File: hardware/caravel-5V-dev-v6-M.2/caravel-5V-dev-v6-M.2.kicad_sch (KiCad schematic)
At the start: 75 parts, among them J1 USB_B_Micro - 10118193-0001LF, J10 Conn_01x02_Male, J11 Conn_01x20_Female, J12 Conn_01x27_Female, J13 Conn_01x02_Male, J2 Conn_01x02_Female, J3 Conn_01x02_Male, J4 Conn_01x03_Female, J5 Conn_01x02_Male, J6 Conn_01x02_Male, J7 Conn_01x06_Female, J8 Conn_01x02_Male, J9 Conn_01x02_Male, SW1 SW_Push - SKQGADE010, T1 Logo, T2 Logo, U1 FT232H, U10 TXB0104PWR, U2 SN74LVC1G125DCKR, U3 SN74LVC1G125DCKR, U4 MCP1319MT-29LE-OT, U5 TAR5SxxU_SOT353F, U6 TXB0104PWR, U7 W25Q32FVSS, U8 caravel-M.2-card, U9 TXB0104PWR, X1 SG7050CCN_10MHZ, Y1 CSTNE12M0GH5L000R0

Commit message: update 5V development board (REV 6B) schematic: ~ fix the reversed connections on the U10 level shifter + add 1 and 0.01 uF bypass caps to the Flash memory supply + add 10 uF bulk decoupling cap to the FTDI supply + add 100K pull-up resistor on the ~{MR} ~ update pull-up resistors of the Flash and ~{UART_EN} to 100K ~ update LEDs resistors to 10K
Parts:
- removed R17, R18: 10k - RC0805FR-0710KL, Resistor_SMD:R_0805_2012Metric, symbol Device:R
- added C23, C25: 0.1uf - CC0805KRX7R9BB104, Capacitor_SMD:C_0805_2012Metric, symbol Device:C
- added C26: 0.01uf - CC0805KRX7R9BB103, Capacitor_SMD:C_0805_2012Metric, symbol Device:C
- added C27: 1uf - CC0805KKX5R8BB105, Capacitor_SMD:C_0805_2012Metric, symbol Device:C
- added U11: MCP1319MT-29LE-OT, Caravel_Board:PoR_5_SOT23, symbol Caravel_board:MCP1319MT-29LE-OT
- C16: value 0.1uf - CC0805KRX7R9BB104 -> 10uf - CC0805KKX5R8BB106
- J10, J13, J3, J5, J6, J8, J9: value Conn_01x02_Male -> Conn_01x02_Pin; symbol Connector:Conn_01x02_Male -> Connector:Conn_01x02_Pin
- J11, J12: symbol Connector:Conn_01x28_Female -> Connector:Conn_01x28_Socket
- J2: symbol Connector:Conn_01x02_Female -> Connector:Conn_01x02_Socket
- J7: symbol Connector:Conn_01x06_Female -> Connector:Conn_01x06_Socket
- R10, R11, R16, R5, R6, R7, R8: value 10k - RC0805FR-0710KL -> 100K - RC0805FR-07100KL
- R13, R14: value 1K - RC0805FR-071KL -> 10k - RC0805FR-0710KL
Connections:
- net +5V: now also R16.1
- net GND: now also C16.1, C23.1, C25.2, C26.1, C27.2, U11.2 (VSS); no longer C16.2
- net USB_SCK_TXD_H: now also U10.10 (B4); no longer U10.11 (B3)
- net USB_SO_RXD_H: now also U10.11 (B3); no longer U10.10 (B4)
- net ~{MR}: now also R16.2
- net at C1.2, U1.34 (~{RESET}): now also R1.2; no longer R1.1
- net OE: now reaches U10.8 (OE)
- net OE: now also U6.8 (OE), U9.8 (OE), U11.1 (~{RST})
- net +3.3V renamed +3V3
- net +3V3: now also C16.2, R1.1, C23.2, C25.1, C26.2, C27.1, U11.5 (VDD); no longer C16.1, R1.2, R16.1
- net UART_EN renamed ~{UART_EN}
- net UART_EN_L renamed ~{UART_EN}_L
- no-connect marks 26 -> 28
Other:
- note added: "Caravel M.2 Card"
- note added: "FTDI SPI interface with HKSPI"
- note added: "FTDI UART interface with Caravel"
- note added: "Flash memory interface with Caravel Flash SPI"
- note added: "GPIO Connectors"
- note added: "Interfaces"
- note added: "Pin Headers"
- note added: "Power Supplies"
- note added: "Reset Switch"
- note removed: "FTDI interface with HKSPI"
- note removed: "Flash memory interface with Caravel"
- note removed: "IO Connectors"
- note removed: "Power Pin Headers"
- moved on the sheet: C1, C10, C11, C12, C13, C14, C15, C17, C18, C19, C2, C20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

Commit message: update `caravel-5V-dev-v6-M.2` to REV6B that fixes identified issues during bringup
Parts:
- removed C17, C18, C19, C20, C23: 0.1uf - CC0805KRX7R9BB104, Capacitor_SMD:C_0805_2012Metric, symbol Device:C
- removed U10, U6, U9: TXB0104PWR, Package_SO:TSSOP-14_4.4x5mm_P0.65mm, symbol Logic_LevelTranslator:TXB0104PW
- removed U11: MCP1319MT-29LE-OT, Caravel_Board:PoR_5_SOT23, symbol Caravel_board:MCP1319MT-29LE-OT
- added C13: 0.01uF, Capacitor_SMD:C_0805_2012Metric, symbol Device:C
- added FB1: 600R/0.5A, Inductor_SMD:L_0805_2012Metric, symbol Device:FerriteBead
- added J14, J15, J16: Conn_01x02_Pin, Connector_PinHeader_2.54mm:PinHeader_1x02_P2.54mm_Vertical, symbol Connector:Conn_01x02_Pin
- added Q1: IRLML6402, Package_TO_SOT_SMD:SOT-23, symbol Transistor_FET:IRLML6402
- added R17, R19: 10K, Resistor_SMD:R_0805_2012Metric, symbol Device:R
- added R18: 2K, Resistor_SMD:R_0805_2012Metric, symbol Device:R
- added R20: 100K, Resistor_SMD:R_0805_2012Metric, symbol Device:R
- added U10, U11, U12, U6, U9: SN74LV1T34DCK, Package_TO_SOT_SMD:SOT-353_SC-70-5, symbol Logic_LevelTranslator:SN74LV1T34DCK
- C1: value 0.01uf - CC0805JRX7R9BB103 -> 0.01uF; Part # (none) -> C0805C103K5RAC7411
- C10: value 1uf - CC0805KKX5R8BB105 -> 1uf; Part # (none) -> 885012207103
- C11: value 0.01uf - CC0805KRX7R9BB103 -> 0.01uF; Part # (none) -> C0805C103K5RAC7411
- C12: value 10uf - CC0805KKX5R8BB106 -> 10uf; Part # (none) -> CL21B106KAYQNNE
- C14: renamed from C13; value 0.1uf - CC0805KRX7R9BB104 -> 0.1uF; Part # (none) -> C0805C104K5RAC7411
- C15, C2, C21, C22, C3, C4, C5, C6, C7, C8, C9: value 0.1uf - CC0805KRX7R9BB104 -> 0.1uF; Part # (none) -> C0805C104K5RAC7411
- C16: renamed from C25; value 0.1uf - CC0805KRX7R9BB104 -> 0.1uF; Part # (none) -> C0805C104K5RAC7411
- C17: renamed from C26; value 0.01uf - CC0805KRX7R9BB103 -> 0.01uF; Part # (none) -> C0805C103K5RAC7411
- C18: renamed from C27; value 1uf - CC0805KKX5R8BB105 -> 1uf; Part # (none) -> 885012207103
- C19: renamed from C16; value 10uf - CC0805KKX5R8BB106 -> 10uf; Part # (none) -> CL21B106KAYQNNE
- C20: renamed from C14; value 10uf - CC0805KKX5R8BB106 -> 10uf; Part # (none) -> CL21B106KAYQNNE
- D1, D2, D3, D4: value LED - 17-215SURC/S530-A2/TR8 -> RED; Part # (none) -> LTST-C230KRKT
- J1: value USB_B_Micro - 10118193-0001LF -> USB_B_Micro; Part # (none) -> 10118193-0001LF
- J11: value Conn_01x20_Female -> Conn_01x28_Pin; footprint Connector_PinHeader_2.54mm:PinHeader_1x20_P2.54mm_Vertical -> Connector_PinHeader_2.54mm:PinHeader_1x28_P2.54mm_Vertical
- J12: value Conn_01x27_Female -> Conn_01x28_Pin; footprint Connector_PinHeader_2.54mm:PinHeader_1x27_P2.54mm_Vertical -> Connector_PinHeader_2.54mm:PinHeader_1x28_P2.54mm_Vertical
- J2: value Conn_01x02_Female -> Conn_01x02_Pin; symbol Connector:Conn_01x02_Socket -> Connector:Conn_01x02_Pin
- J4: value Conn_01x03_Female -> Conn_01x03_Pin
- J7: value Conn_01x06_Female -> Conn_01x06_Pin; symbol Connector:Conn_01x06_Socket -> Connector:Conn_01x06_Pin
- R1, R12, R13, R14, R15, R9: value 10k - RC0805FR-0710KL -> 10K; Part # (none) -> RC0805FR-0710KL
- R10, R11, R7, R8: value 100K - RC0805FR-07100KL -> 100K; Part # (none) -> RC0805FR-07100KL
- R16, R5, R6: value 100K - RC0805FR-07100KL -> 10K; Part # (none) -> RC0805FR-0710KL
- R2: value 12K 1% - 0805W8F1202T5E -> 12K 1%; Part # (none) -> RMCF0805FT12K0
- R3, R4: value 150 - 0805W8J0151T5E -> 150; Part # (none) -> RNCP0805FTD150R
- U1: Part # (none) -> FT232H
- U2, U3: Field4 76C4082 -> (none); Field5 Texas Instruments -> (none); Field6 SN74LVC1G125DCKR -> (none); Field7 1470771 -> (none); Part # (none) -> SN74LVC1G125DCKR
- U4: Part # (none) -> MCP1319MT-29LE-OT
- U5: value TAR5SxxU_SOT353F -> TAR5SxxU; Part # (none) -> TAR5S33UTE85LF
- U7: Part # (none) -> W25Q32JVSSIQ
- U8: value caravel-M.2-card -> M.2-CONNECTOR-E; symbol Caravel_board:caravel-M.2-card -> MicroMod-Sparkfun:M.2-CONNECTOR-E
- X1: Part # (none) -> SG7050CCN-10-000000M-HJGA3
- Y1: value CSTNE12M0GH5L000R0 -> 12MHz; Part # (none) -> CSTNE12M0GH5L000R0
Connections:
- net USB_SCK_TXD_H is gone; now on net USB_SCK_TXD: U3.2 (A)
- net USB_SO_RXD_H is gone; now on net USB_SO_RXD: U2.4 (Y)
- net mprj_io[1]_SDO is gone; now on net USB_SI: J11.14 (Pin_14), U8.51 (P43)
- net mprj_io[2]_SDI is gone; now on net USB_SO_RXD: J11.13 (Pin_13), U8.53 (P45)
- net mprj_io[3]_CSB is gone; now on net USB_CS1: J11.12 (Pin_12), U8.55 (P47)
- net mprj_io[4]_SCK is gone; now on net USB_SCK_TXD: J11.11 (Pin_11), U8.57 (P49)
- net ~{MR}_L is gone; now on net ~{MR}: U1.25 (ACBUS1)
- net ~{UART_EN}_L is gone; now on net ~{UART_EN}: U1.21 (ACBUS0)
- net +3V3: now also C19.1, C4.1, C5.1, C6.1, C7.1, C8.1, R5.1, R6.1, U2.5 (VCC), U3.5 (VCC), R20.1, U10.5 (VCC), U6.5 (VCC), U9.5 (VCC); no longer C19.2, C21.2, C4.2, C5.2, C6.2, C7.2, C8.2
- net +5V: now also C14.2, C15.1, FB1.2, Q1.2 (S), R17.2, U11.5 (VCC), U12.5 (VCC); no longer C14.1, C15.2, C22.2, J1.1 (VBUS), J10.1 (Pin_1), J10.2 (Pin_2), J11.22 (Pin_22), J11.23 (Pin_23), J11.24 (Pin_24), J12.7 (Pin_7), J13.1 (Pin_1), J13.2 (Pin_2), J3.1 (Pin_1), J3.2 (Pin_2), J5.1 (Pin_1), J5.2 (Pin_2), J9.1 (Pin_1), J9.2 (Pin_2), R5.1, R6.1, U2.5 (VCC), U3.5 (VCC), U8.14 (vccd), U8.15 (vcdd), U8.16 (vddio), U8.3 (vddio), U8.35 (vccd1), U8.5 (vdda)
- net Caravel_CSB: now also U6.2 (A)
- net Caravel_D0: now also U10.2 (A)
- net Caravel_D1: now also U11.4 (Y)
- net Caravel_SCK: now also U9.2 (A)
- net GND: now also C14.1, C15.2, C19.2, C4.2, C5.2, C6.2, C7.2, C8.2, C13.2, R19.1, U10.3 (GND), U11.3 (GND), U12.3 (GND), U6.3 (GND), U9.3 (GND); no longer C14.2, C15.1, C19.1, C21.1, C4.1, C5.1, C6.1, C7.1, C8.1
- net MEM_SCK: now also U9.4 (Y)
- net MEM_SI: now also U10.4 (Y)
- net MEM_SO: now also U11.2 (A)
- net USB_SI: now also J16.1 (Pin_1), J16.2 (Pin_2), R20.2
- net ~{MR}: now also J14.2 (Pin_2)
- net ~{RST}: now also J14.1 (Pin_1)
- net VCCA: now reaches C3.2, U1.37 (VCCA)
- net Noise: now reaches C11.1, U5.3 (Noise)
- net ~{FTDI_RST}: now reaches C1.2, R1.2, U1.34 (~{RESET})
- net VCCCORE: now reaches C2.2, U1.38 (VCCCORE)
- net ~{PWR_EN}: now reaches U1.33 (ACBUS9)
- net ~{PWR_EN}: now also J15.1 (Pin_1), J15.2 (Pin_2), R19.2, U12.2 (A)
- net MEM_CS renamed ~{MEM_CS}
- net ~{MEM_CS}: now also U6.4 (Y)
- new net: C21.1, Q1.1 (G), R17.1, R18.2
- new net VBUS: C13.1, FB1.1, J1.1 (VBUS), J13.1 (Pin_1), J13.2 (Pin_2)
- new net VCC: C21.2, C22.2, J10.1 (Pin_1), J10.2 (Pin_2), J11.22 (Pin_22), J11.23 (Pin_23), J11.24 (Pin_24), J12.7 (Pin_7), J3.1 (Pin_1), J3.2 (Pin_2), J5.1 (Pin_1), J5.2 (Pin_2), J9.1 (Pin_1), J9.2 (Pin_2), Q1.3 (D), U8.14 (P14), U8.15 (P15), U8.16 (P16), U8.3 (P3), U8.35 (P27), U8.5 (P5)
- new net ~{PWR_EN}_H: R18.1, U12.4 (Y)
- no-connect marks 28 -> 25
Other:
- note added: "*Caravel power is turned on by default and the FTDI controls ~{PWR_EN}"
- note added: "*J16 ensures HKSPI SDO state when it's left high-impedance"
- note added: "*Place close to the USB connector"
- note added: "*required since the FTDI UART ports are shared with the SPI"
- note added: "*skips installing the PoR"
- note added: "Buffers to enable FTDI UART interface with Caravel"
- note added: "M.2 Connector + Peripherals"
- note added: "Power"
- note added: "Power Cycle Control"
- note added: "Reset"
- note added: "Reset Pin Header"
- note added: "USB to Serial"
- note added: "Use J15 to control it externally"
- note added: "VBUS Filter to 5V"
- note removed: "Buffers to enable FTDI UART interface"
- note removed: "FTDI UART interface with Caravel"
- note removed: "Power Supplies"
- company: (none) -> Efabless
- title: (none) -> 5V Development Board
- moved on the sheet: C1, C10, C11, C12, C14, C15, C16, C17, C18, C19, C2, C20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

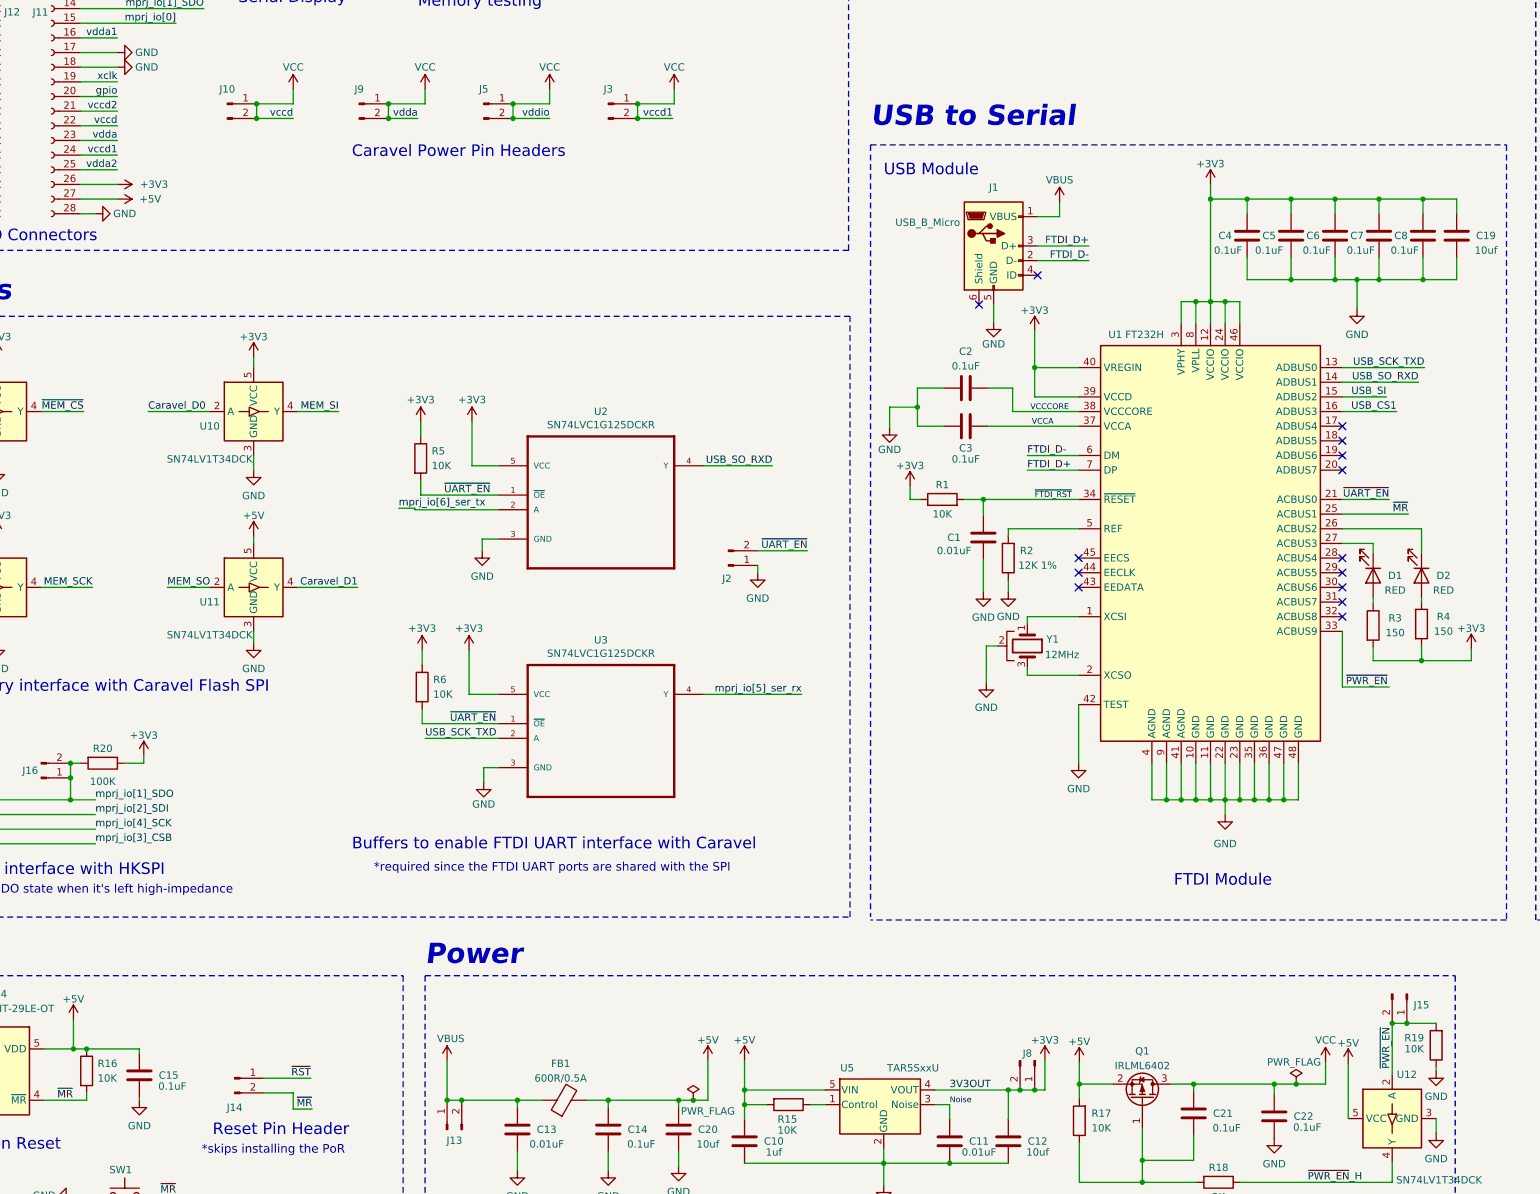
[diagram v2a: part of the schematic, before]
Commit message: update `caravel-5V-dev-v6-M.2` (REV6B) + add an 0.1uF bypass cap to the Flash level shifters ~ update BOM
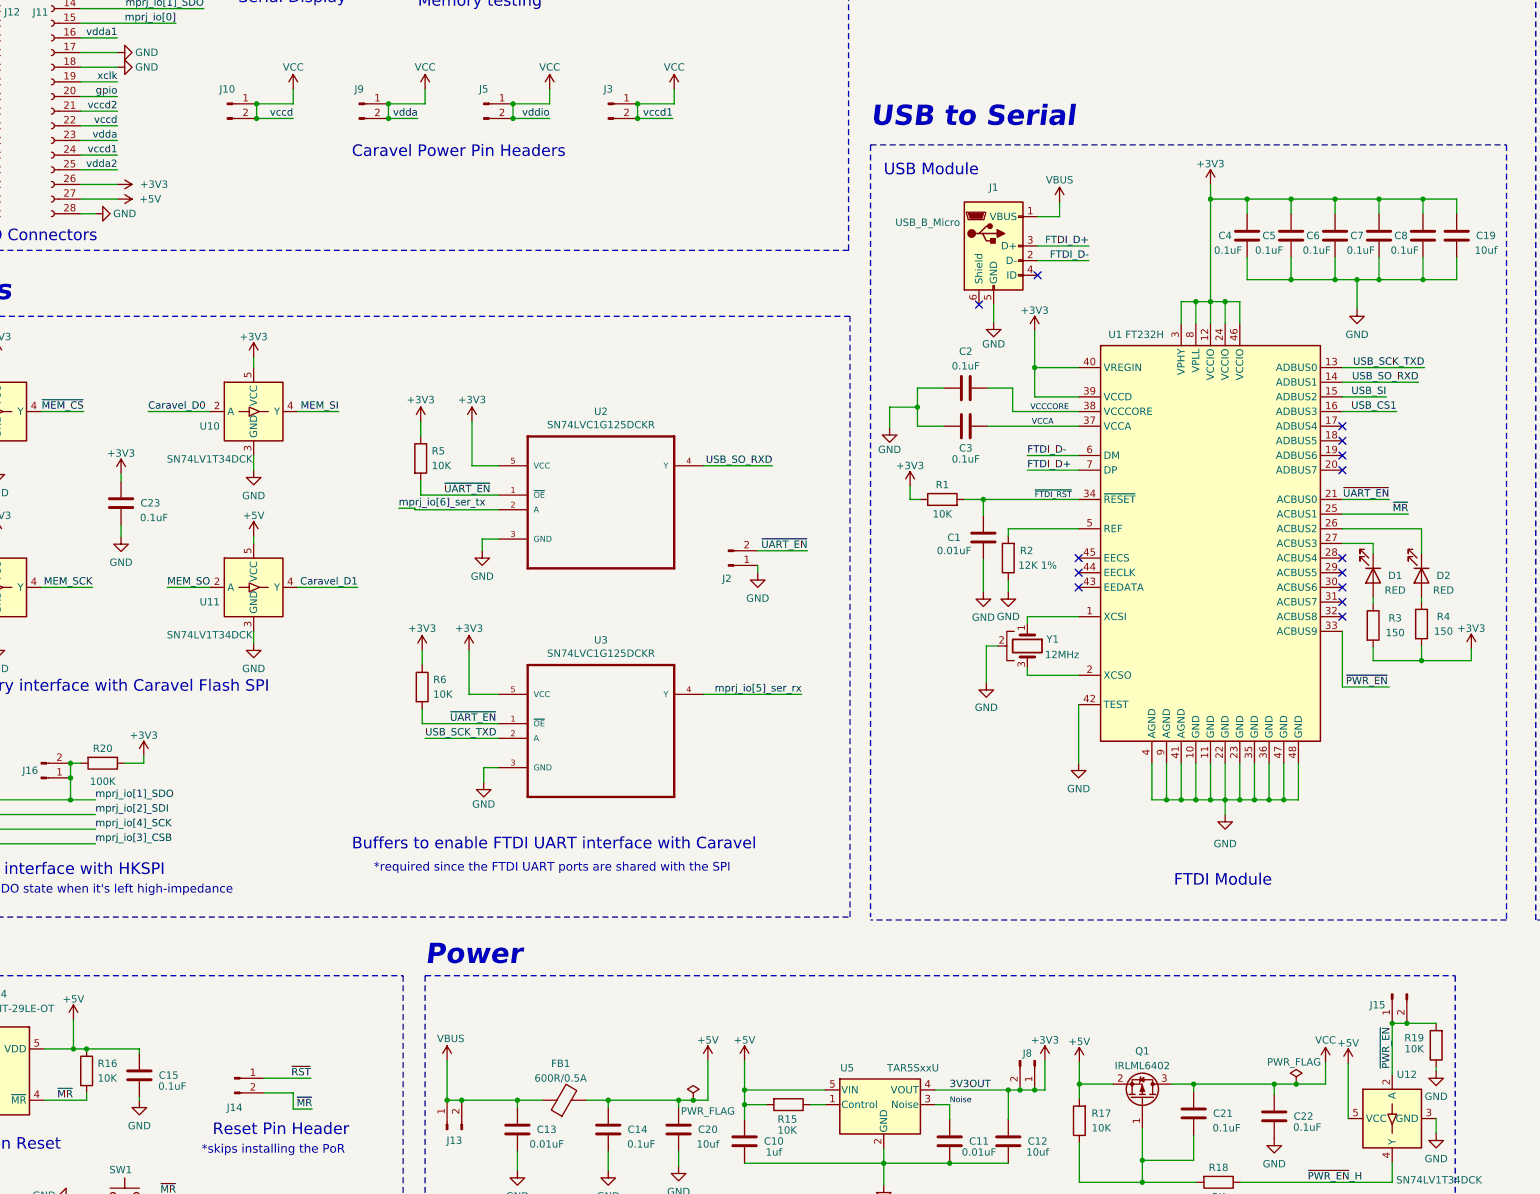
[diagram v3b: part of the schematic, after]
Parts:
- added C23: 0.1uF, Capacitor_SMD:C_0805_2012Metric, symbol Device:C
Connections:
- net +3V3: now also C23.2
- net GND: now also C23.1
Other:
- moved on the sheet: J15
